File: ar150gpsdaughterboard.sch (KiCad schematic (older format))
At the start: 7 parts, among them P1 CONN_02X05, Q1 BSS138, U1 QUECTEL-L80

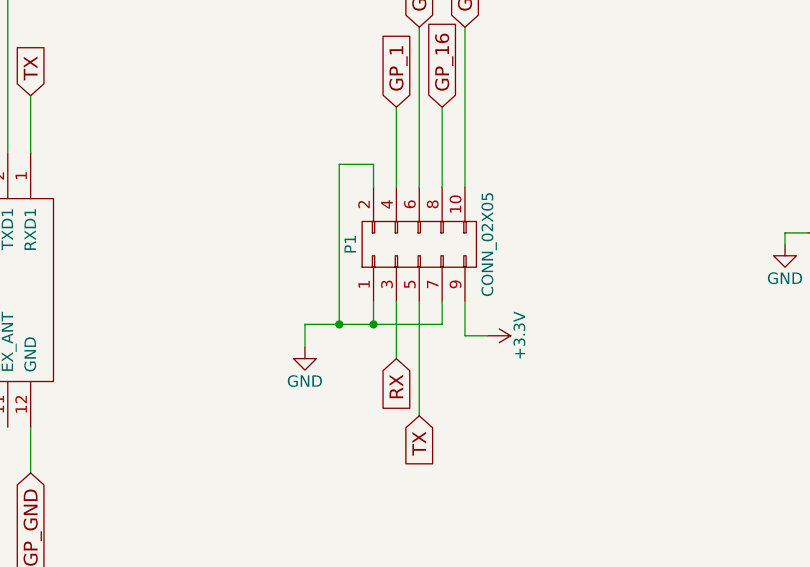
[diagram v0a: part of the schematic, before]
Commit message: updated pinout of the ar150 pin header
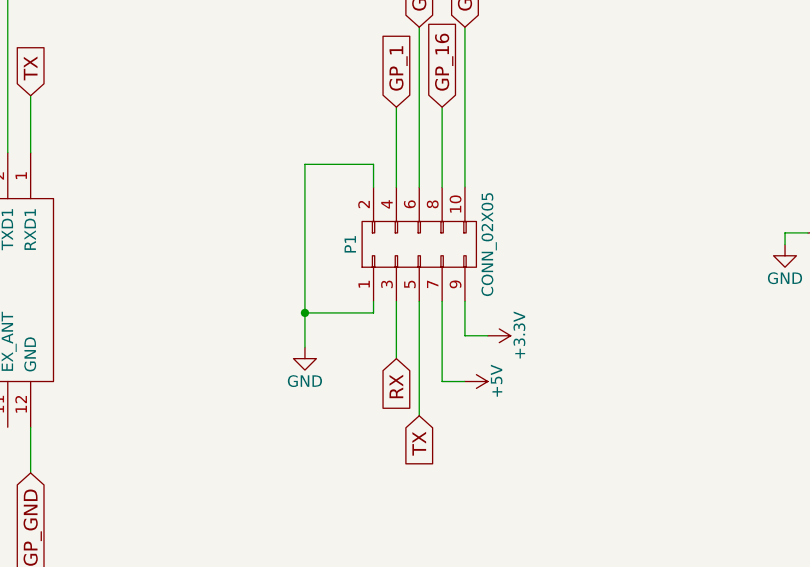
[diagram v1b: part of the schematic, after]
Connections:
- net GND: no longer P1.7 (P7)
- new net +5V: P1.7 (P7)
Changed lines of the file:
@@
 	1    0    0    -1
 $EndComp
-Wire Wire Line
-	3700 2600 3700 2700
-Wire Wire Line
-	3400 2700 4000 2700
-Wire Wire Line
-	3400 2700 3400 2800
-Wire Wire Line
-	4000 2700 4000 2600
-Connection ~ 3700 2700
-Wire Wire Line
-	3700 2100 3700 2000
-Wire Wire Line
-	3700 2000 3550 2000
-Wire Wire Line
-	3550 2000 3550 2700
-Connection ~ 3550 2700
 $Comp
 L +3.3V #PWR02
@@
 	1800 1700 1900 1700
 Connection ~ 1900 1700
+Wire Wire Line
+	3700 2600 3700 2650
+Wire Wire Line
+	3700 2650 3400 2650
+Wire Wire Line
+	3400 2000 3400 2800
+Wire Wire Line
+	3700 2100 3700 2000
+Wire Wire Line
+	3700 2000 3400 2000
+Connection ~ 3400 2650
+$Comp
+L +5V #PWR?
+U 1 1 5939F455
+P 4100 2950
+F 0 "#PWR?" H 4100 2800 50  0001 C CNN
+F 1 "+5V" H 4100 3090 50  0000 C CNN
+F 2 "" H 4100 2950 50  0000 C CNN
+F 3 "" H 4100 2950 50  0000 C CNN
+	1    4100 2950
+	0    1    1    0
+$EndComp
+Wire Wire Line
+	4000 2600 4000 2950
+Wire Wire Line
+	4000 2950 4100 2950
 $EndSCHEMATC

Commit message: new board with a pps line indicator
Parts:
- added D3: LED, LEDs:LED_0805, symbol LED
- added R3: 300, Resistors_SMD:R_0805, symbol R
- R1, R2: value R -> 300
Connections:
- net GND: now also D3.1 (K)
- net GP_14: now also R3.1
- new net: D3.2 (A), R3.2
- no-connect marks 1 -> 2
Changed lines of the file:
@@
 $EndComp
 $Comp
-L GND #PWR01
+L GND #PWR4
 U 1 1 5911098B
 P 3400 2800
-F 0 "#PWR01" H 3400 2550 50  0001 C CNN
+F 0 "#PWR4" H 3400 2550 50  0001 C CNN
 F 1 "GND" H 3400 2650 50  0000 C CNN
 F 2 "" H 3400 2800 50  0000 C CNN
@@
 $EndComp
 $Comp
-L +3.3V #PWR02
+L +3.3V #PWR6
 U 1 1 591109C2
 P 4200 2750
-F 0 "#PWR02" H 4200 2600 50  0001 C CNN
+F 0 "#PWR6" H 4200 2600 50  0001 C CNN
 F 1 "+3.3V" H 4200 2890 50  0000 C CNN
 F 2 "" H 4200 2750 50  0000 C CNN
@@
 P 2500 4800
 F 0 "R1" V 2580 4800 50  0000 C CNN
-F 1 "R" V 2500 4800 50  0000 C CNN
+F 1 "300" V 2500 4800 50  0000 C CNN
 F 2 "Resistors_SMD:R_0805" V 2430 4800 50  0001 C CNN
 F 3 "" H 2500 4800 50  0000 C CNN
@@
 P 2500 5350
 F 0 "R2" V 2580 5350 50  0000 C CNN
-F 1 "R" V 2500 5350 50  0000 C CNN
+F 1 "300" V 2500 5350 50  0000 C CNN
 F 2 "Resistors_SMD:R_0805" V 2430 5350 50  0001 C CNN
 F 3 "" H 2500 5350 50  0000 C CNN
@@
 $EndComp
 $Comp
-L GND #PWR03
+L GND #PWR1
 U 1 1 59110D10
 P 1550 4800
-F 0 "#PWR03" H 1550 4550 50  0001 C CNN
+F 0 "#PWR1" H 1550 4550 50  0001 C CNN
 F 1 "GND" H 1550 4650 50  0000 C CNN
 F 2 "" H 1550 4800 50  0000 C CNN
@@
 	2350 4800 2100 4800
 $Comp
-L +3.3V #PWR04
+L +3.3V #PWR3
 U 1 1 59110E67
 P 2750 4700
-F 0 "#PWR04" H 2750 4550 50  0001 C CNN
+F 0 "#PWR3" H 2750 4550 50  0001 C CNN
 F 1 "+3.3V" H 2750 4840 50  0000 C CNN
 F 2 "" H 2750 4700 50  0000 C CNN
@@
 	5750 1900 5750 2000
 $Comp
-L GND #PWR05
+L GND #PWR8
 U 1 1 59110F7C
 P 5500 2350
-F 0 "#PWR05" H 5500 2100 50  0001 C CNN
+F 0 "#PWR8" H 5500 2100 50  0001 C CNN
 F 1 "GND" H 5500 2200 50  0000 C CNN
 F 2 "" H 5500 2350 50  0000 C CNN
@@
 TX
 $Comp
-L +3.3V #PWR06
+L +3.3V #PWR2
 U 1 1 591136CE
 P 1900 1250
-F 0 "#PWR06" H 1900 1100 50  0001 C CNN
+F 0 "#PWR2" H 1900 1100 50  0001 C CNN
 F 1 "+3.3V" H 1900 1390 50  0000 C CNN
 F 2 "" H 1900 1250 50  0000 C CNN
@@
 Connection ~ 3400 2650
 $Comp
-L +5V #PWR?
+L +5V #PWR5
 U 1 1 5939F455
 P 4100 2950
-F 0 "#PWR?" H 4100 2800 50  0001 C CNN
+F 0 "#PWR5" H 4100 2800 50  0001 C CNN
 F 1 "+5V" H 4100 3090 50  0000 C CNN
 F 2 "" H 4100 2950 50  0000 C CNN
@@
 Wire Wire Line
 	4000 2950 4100 2950
+Text GLabel 3650 4800 0    60   Input ~ 0
+GP_14
+$Comp
+L R R3
+U 1 1 593D3915
+P 4000 4800
+F 0 "R3" V 4080 4800 50  0000 C CNN
+F 1 "300" V 4000 4800 50  0000 C CNN
+F 2 "Resistors_SMD:R_0805" V 3930 4800 50  0001 C CNN
+F 3 "" H 4000 4800 50  0000 C CNN
+	1    4000 4800
+	0    -1   -1   0
+$EndComp
+$Comp
+L LED D3
+U 1 1 593D397F
+P 4500 4800
+F 0 "D3" H 4500 4900 50  0000 C CNN
+F 1 "LED" H 4500 4700 50  0000 C CNN
+F 2 "LEDs:LED_0805" H 4500 4800 50  0001 C CNN
+F 3 "" H 4500 4800 50  0000 C CNN
+	1    4500 4800
+	-1   0    0    1
+$EndComp
+$Comp
+L GND #PWR7
+U 1 1 593D3A06
+P 4950 4800
+F 0 "#PWR7" H 4950 4550 50  0001 C CNN
+F 1 "GND" H 4950 4650 50  0000 C CNN
+F 2 "" H 4950 4800 50  0000 C CNN
+F 3 "" H 4950 4800 50  0000 C CNN
+	1    4950 4800
+	0    -1   -1   0
+$EndComp
+Wire Wire Line
+	3650 4800 3850 4800
+Wire Wire Line
+	4150 4800 4300 4800
+Wire Wire Line
+	4700 4800 4950 4800
+NoConn ~ 4850 5300
 $EndSCHEMATC
